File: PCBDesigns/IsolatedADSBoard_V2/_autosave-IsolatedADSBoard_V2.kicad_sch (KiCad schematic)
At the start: 18 parts, among them J1 Screw_Terminal_01x06, J2 Screw_Terminal_01x08, J3 Conn_01x04_MountingPin, U1 ADuM1200AR, U13 ISO1540, U14 RFM-0505S, U3 ADS1115IDGS

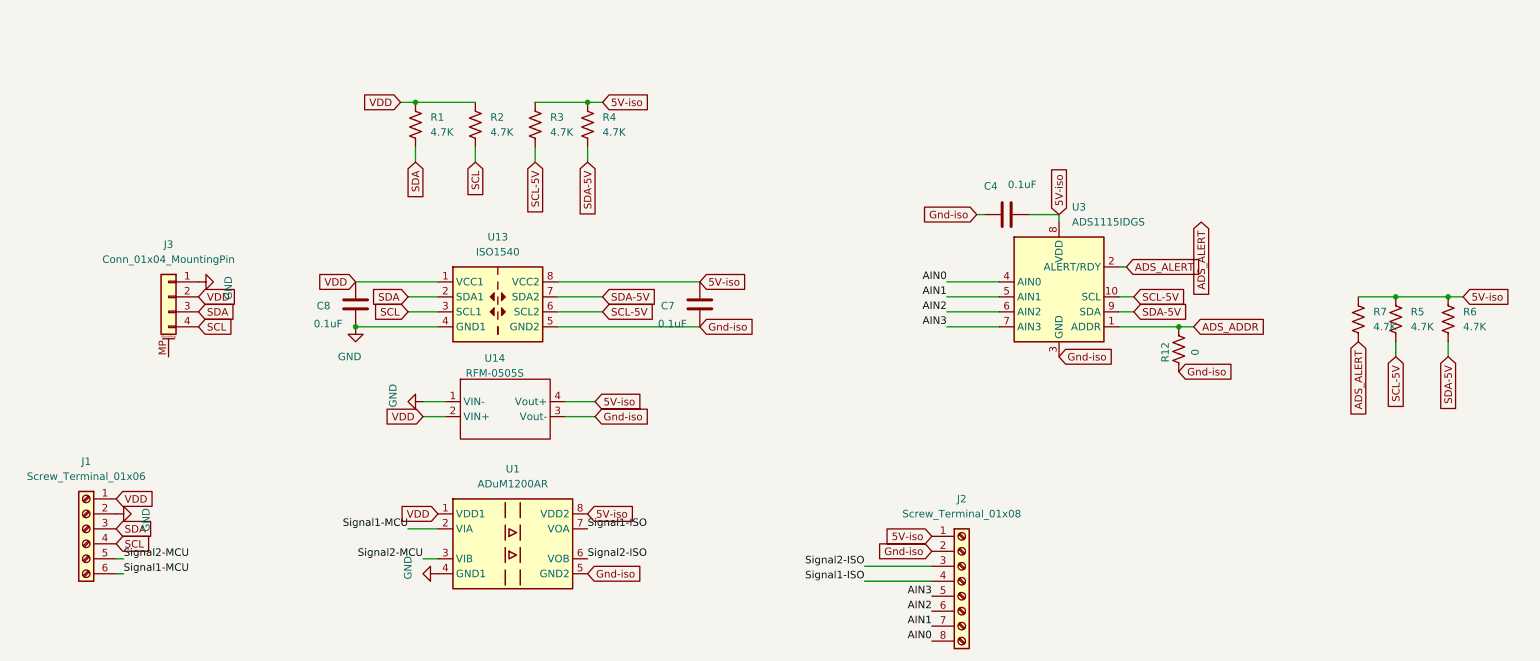
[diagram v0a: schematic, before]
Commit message: Some V2 Isolator PCB work and some radio data tests
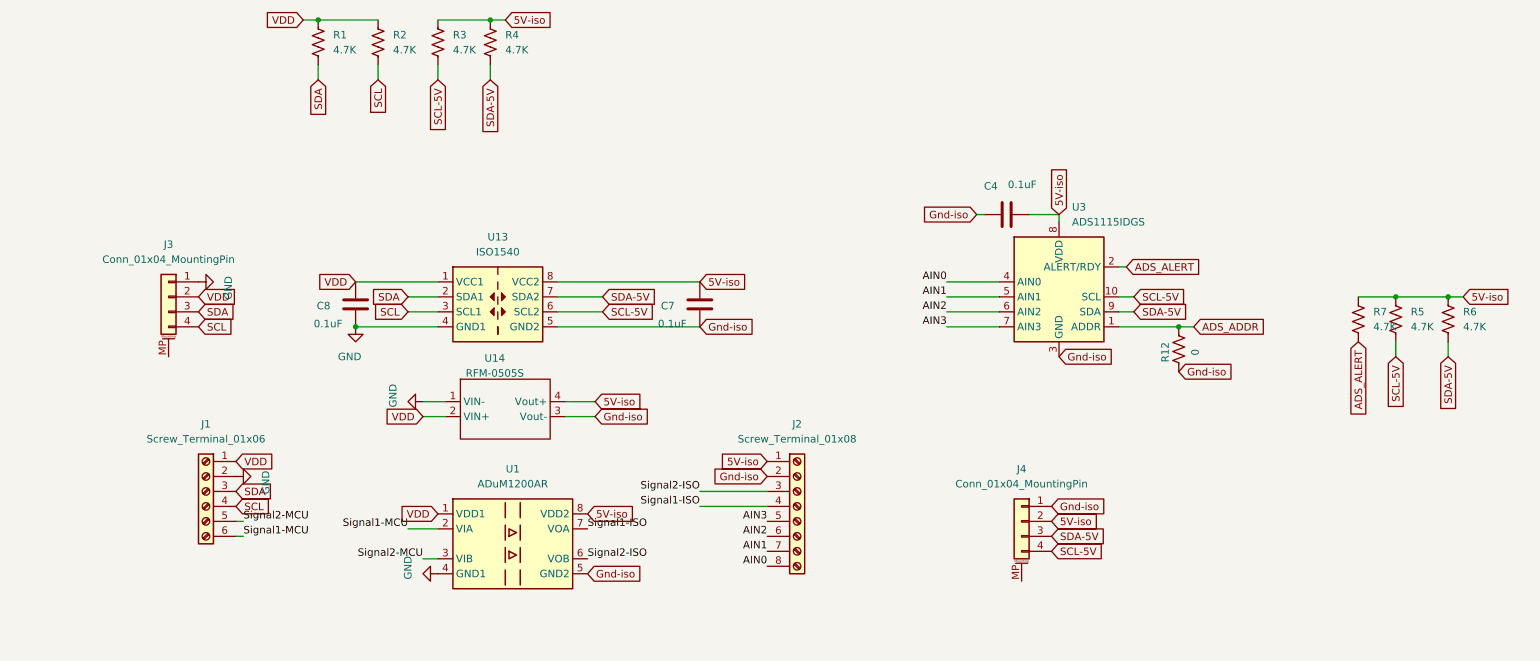
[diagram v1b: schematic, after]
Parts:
- added J4: Conn_01x04_MountingPin, Connector_JST:JST_SH_SM04B-SRSS-TB_1x04-1MP_P1.00mm_Horizontal, symbol Connector_Generic_MountingPin:Conn_01x04_MountingPin
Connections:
- net 5V-iso: now also J4.2 (Pin_2)
- net Gnd-iso: now also J4.1 (Pin_1)
- net SCL-5V: now also J4.4 (Pin_4)
- net SDA-5V: now also J4.3 (Pin_3)
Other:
- moved on the sheet: J1, J2, R1, R2, R3, R4

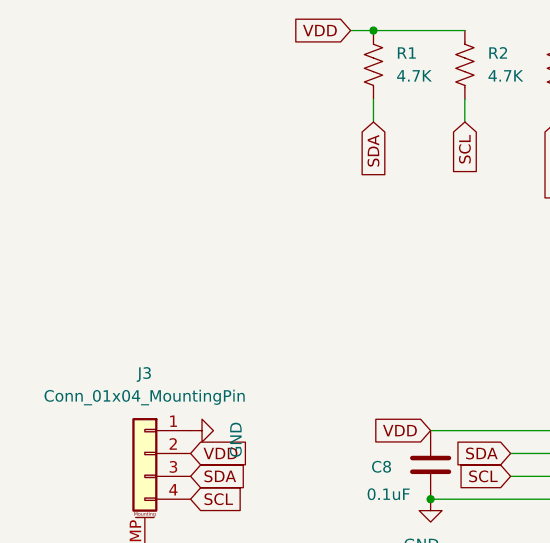
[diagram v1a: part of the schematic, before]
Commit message: Added both a temp sensor and the "mark place" button for the log
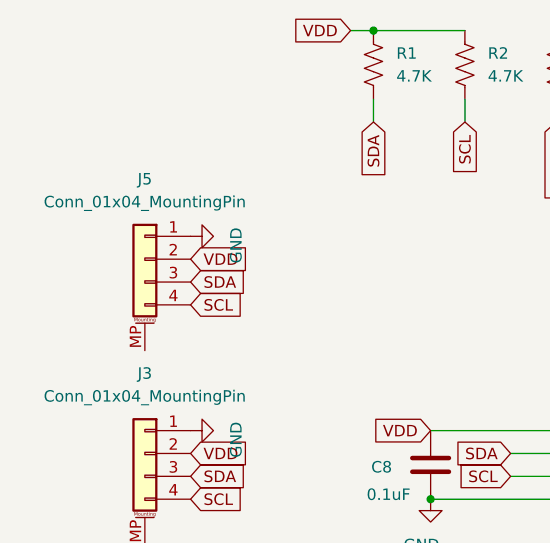
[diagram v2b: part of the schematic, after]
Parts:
- added J5: Conn_01x04_MountingPin, Connector_JST:JST_SH_SM04B-SRSS-TB_1x04-1MP_P1.00mm_Horizontal, symbol Connector_Generic_MountingPin:Conn_01x04_MountingPin
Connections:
- net GND: now also J5.1 (Pin_1)
- net SCL: now also J5.4 (Pin_4)
- net SDA: now also J5.3 (Pin_3)
- net VDD: now also J5.2 (Pin_2)
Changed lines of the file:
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@@
 	(global_label "SCL"
 		(shape input)
+		(at 27.94 55.88 0)
+		(fields_autoplaced yes)
+		(effects
+			(font
+				(size 1.27 1.27)
+			)
+			(justify left)
+		)
+		(property "Intersheetrefs" "${INTERSHEET_REFS}"
+			(at 34.4328 55.88 0)
+			(effects
+				(font
+					(size 1.27 1.27)
+				)
+				(justify left)
+				(hide yes)
+			)
+		)
+	)
+	(global_label "SCL"
+		(shape input)
 		(at 63.5 74.93 180)
 		(fields_autoplaced yes)
@@
 		)
 	)
+	(global_label "VDD"
+		(shape input)
+		(at 27.94 50.8 0)
+		(fields_autoplaced yes)
+		(effects
+			(font
+				(size 1.27 1.27)
+			)
+			(justify left)
+		)
+		(property "Intersheetrefs" "${INTERSHEET_REFS}"
+			(at 34.5538 50.8 0)
+			(effects
+				(font
+					(size 1.27 1.27)
+				)
+				(justify left)
+				(hide yes)
+			)
+		)
+	)
 	(global_label "SDA-5V"
 		(shape input)
@@
 		(property "Intersheetrefs" "${INTERSHEET_REFS}"
 			(at 197.0533 72.39 0)
+			(effects
+				(font
+					(size 1.27 1.27)
+				)
+				(justify left)
+				(hide yes)
+			)
+		)
+	)
+	(global_label "SDA"
+		(shape input)
+		(at 27.94 53.34 0)
+		(fields_autoplaced yes)
+		(effects
+			(font
+				(size 1.27 1.27)
+			)
+			(justify left)
+		)
+		(property "Intersheetrefs" "${INTERSHEET_REFS}"
+			(at 34.4933 53.34 0)
 			(effects
 				(font
@@
 	)
 	(symbol
+		(lib_id "power:GND")
+		(at 27.94 48.26 90)
+		(unit 1)
+		(exclude_from_sim no)
+		(in_bom yes)
+		(on_board yes)
+		(dnp no)
+		(property "Reference" "#PWR04"
+			(at 34.29 48.26 0)
+			(effects
+				(font
+					(size 1.27 1.27)
+				)
+				(hide yes)
+			)
+		)
+		(property "Value" "GND"
+			(at 33.02 49.276 0)
+			(effects
+				(font
+					(size 1.27 1.27)
+				)
+			)
+		)
+		(property "Footprint" ""
+			(at 27.94 48.26 0)
+			(effects
+				(font
+					(size 1.27 1.27)
+				)
+				(hide yes)
+			)
+		)
+		(property "Datasheet" ""
+			(at 27.94 48.26 0)
+			(effects
+				(font
+					(size 1.27 1.27)
+				)
+				(hide yes)
+			)
+		)
+		(property "Description" "Power symbol creates a global label with name \"GND\" , ground"
+			(at 27.94 48.26 0)
+			(effects
+				(font
+					(size 1.27 1.27)
+				)
+				(hide yes)
+			)
+		)
+		(pin "1"
+		)
+		(instances
+			(project "IsolatedADSBoard_V2"
+				(path "/948ff3f4-c0c6-4f78-99ba-ed3a397491b6"
+					(reference "#PWR04")
+					(unit 1)
+				)
+			)
+		)
+	)
+	(symbol
 		(lib_id "Connector_Generic_MountingPin:Conn_01x04_MountingPin")
 		(at 22.86 72.39 0)
@@
 					(unit 1)
 				)
+			)
+		)
+	)
+	(symbol
+		(lib_id "Connector_Generic_MountingPin:Conn_01x04_MountingPin")
+		(at 22.86 50.8 0)
+		(mirror y)
+		(unit 1)
+		(exclude_from_sim no)
+		(in_bom yes)
+		(on_board yes)
+		(dnp no)
+		(fields_autoplaced yes)
+		(property "Reference" "J5"
+			(at 22.86 41.91 0)
+			(effects
+				(font
+					(size 1.27 1.27)
+				)
+			)
+		)
+		(property "Value" "Conn_01x04_MountingPin"
+			(at 22.86 44.45 0)
+			(effects
+				(font
+					(size 1.27 1.27)
+				)
+			)
+		)
+		(property "Footprint" "Connector_JST:JST_SH_SM04B-SRSS-TB_1x04-1MP_P1.00mm_Horizontal"
+			(at 22.86 50.8 0)
+			(effects
+				(font
+					(size 1.27 1.27)
+				)
+				(hide yes)
+			)
+		)
+		(property "Datasheet" "~"
+			(at 22.86 50.8 0)
+			(effects
+				(font
+					(size 1.27 1.27)
+				)
+				(hide yes)
+			)
+		)
+		(property "Description" "Generic connectable mounting pin connector, single row, 01x04, script generated (kicad-library-utils/schlib/autogen/connector/)"
+			(at 22.86 50.8 0)
+			(effects
+				(font
+					(size 1.27 1.27)
+				)
+				(hide yes)
+			)
+		)
+		(pin "1"
+		)
+		(pin "2"
+		)
+		(pin "4"
+		)
+		(pin "3"
+		)
+		(pin "MP"
+		)
+		(instances
+			(project "IsolatedADSBoard_V2"
+				(path "/948ff3f4-c0c6-4f78-99ba-ed3a397491b6"
+					(reference "J5")
+					(unit 1)
+				)
